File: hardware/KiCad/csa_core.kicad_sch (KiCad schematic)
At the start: 10 parts, among them Q1 2SK932, U5 AD8099ARD

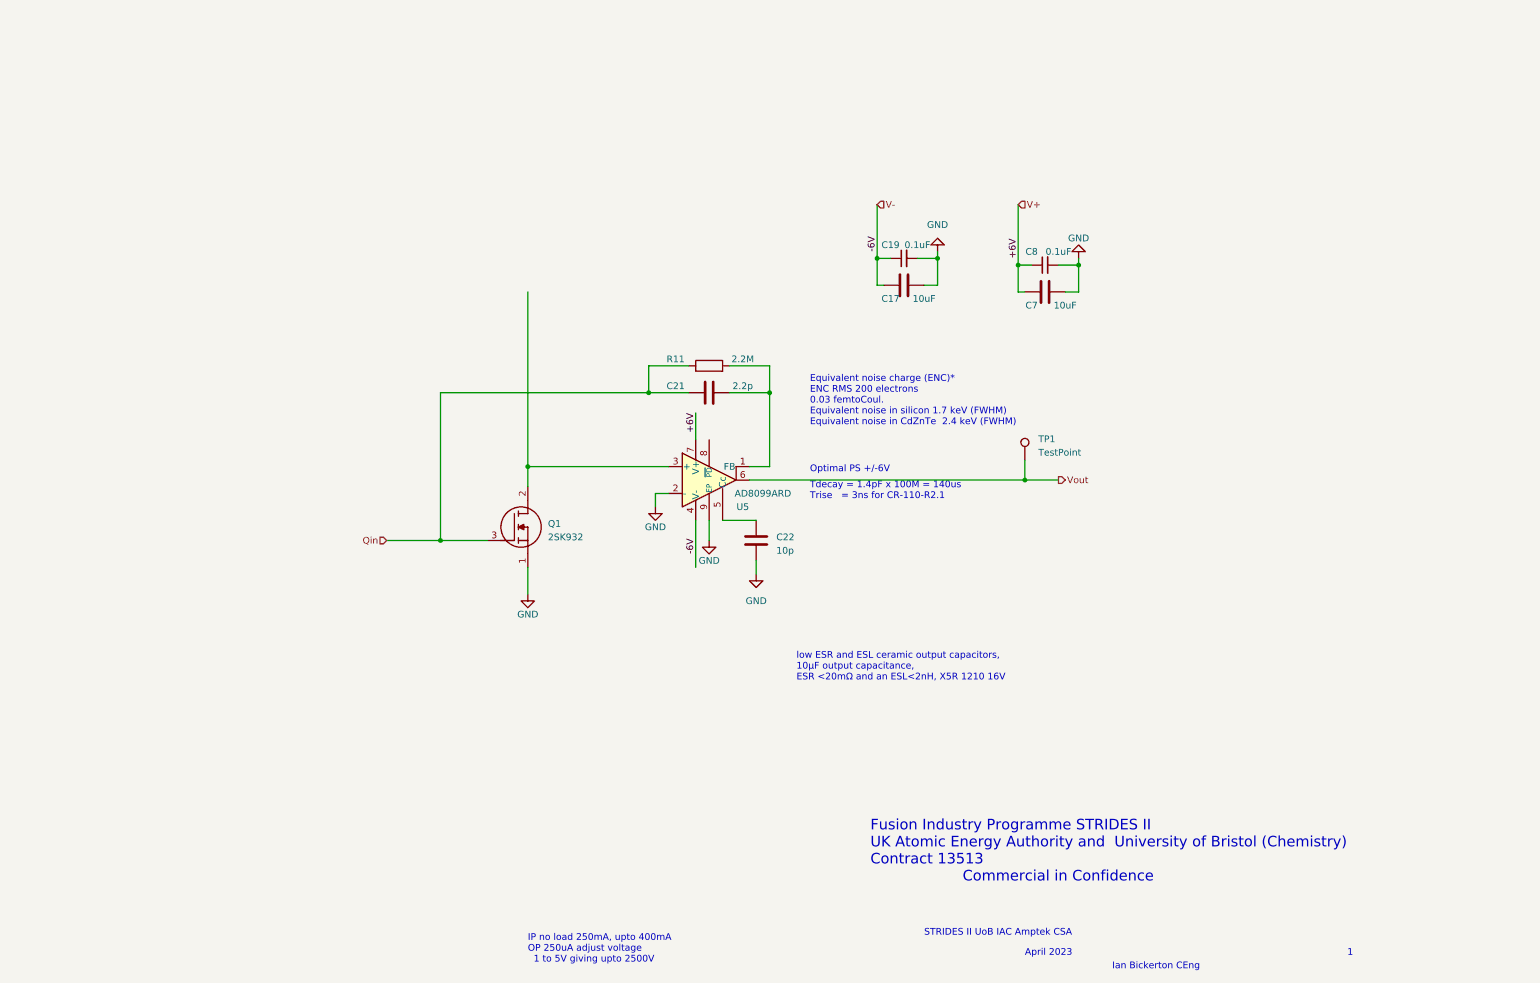
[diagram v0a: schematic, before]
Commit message: More schemataic tidying. Added a csa_core_simulation.kicad_pro to simulate CSA core. Tidied csa_core to make it simulatable, but needs work - OP analysis doesn't converge at the moment. (Need to fiddle with op-amp compensation??)
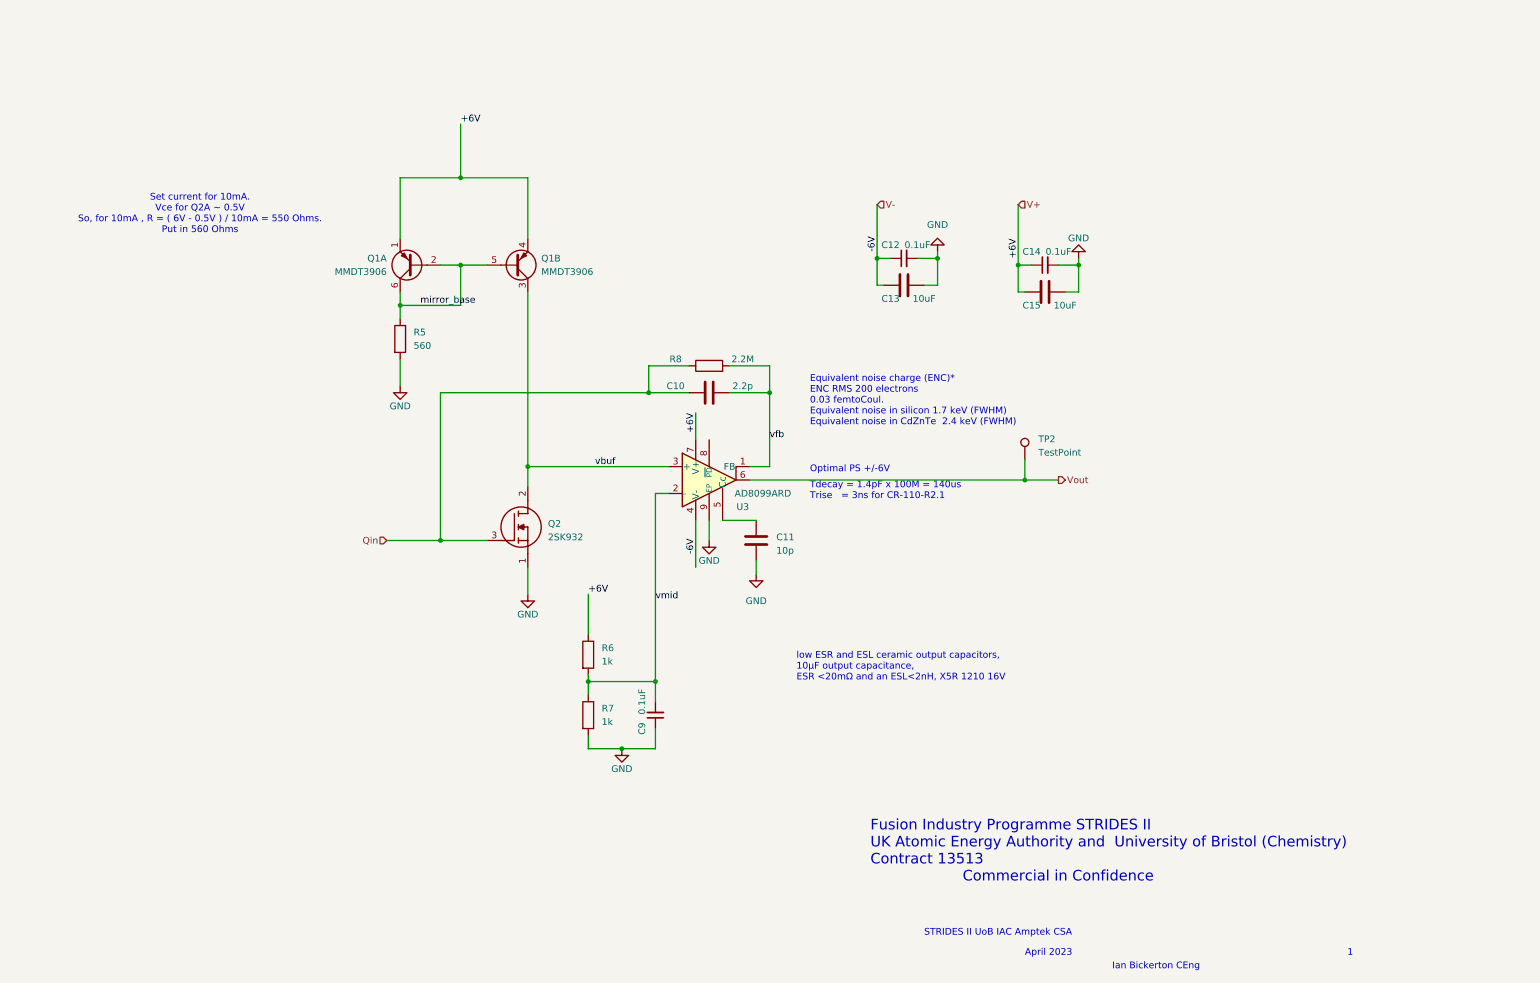
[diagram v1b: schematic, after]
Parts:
- added C9: 0.1uF, Capacitor_SMD:C_0805_2012Metric, symbol Device:C_Small
- added Q1: MMDT3906, Package_TO_SOT_SMD:SOT-363_SC-70-6, symbol Transistor_BJT:MMDT3906
- added R5: 560, Resistor_SMD:R_0603_1608Metric, symbol Device:R
- added R6, R7: 1k, Resistor_SMD:R_0603_1608Metric, symbol Device:R
- C11: renamed from C22; footprint (none) -> Capacitor_SMD:C_0603_1608Metric
- renumbered C21 to C10, C19 to C12, C17 to C13, C8 to C14, C7 to C15, Q1 to Q2, R11 to R8, TP1 to TP2, U5 to U3
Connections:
- net GND: now also C9.1, R5.2, R7.2; no longer U3.2 (-)
- net V+: now also Q1.1 (E1), Q1.4 (E2), R6.1
- net vfb: now reaches C10.2, R8.2, U3.1 (FB)
- net vbuf: now reaches Q2.2 (D), U3.3 (+)
- net vbuf: now also Q1.3 (C2)
- new net mirror_base: Q1.2 (B1), Q1.5 (B2), Q1.6 (C1), R5.1
- new net vmid: C9.2, R6.2, R7.1, U3.2 (-)
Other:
- note added: "Set current for 10mA. Vce for Q2A ~ 0.5V So, for 10mA , R = ( 6V - 0.5V ) / 10mA = 550 Ohms. Put in 560 Ohms"
- note removed: "IP no load 250mA, upto 400mA OP 250uA adjust voltage 1 to 5V giving upto 2500V"

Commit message: Added lead-lag compenstation after JFET which seems to stabilize loop in simulation. Added CR-RC shaping/amplification. Committing changes before starting simulation of shapers
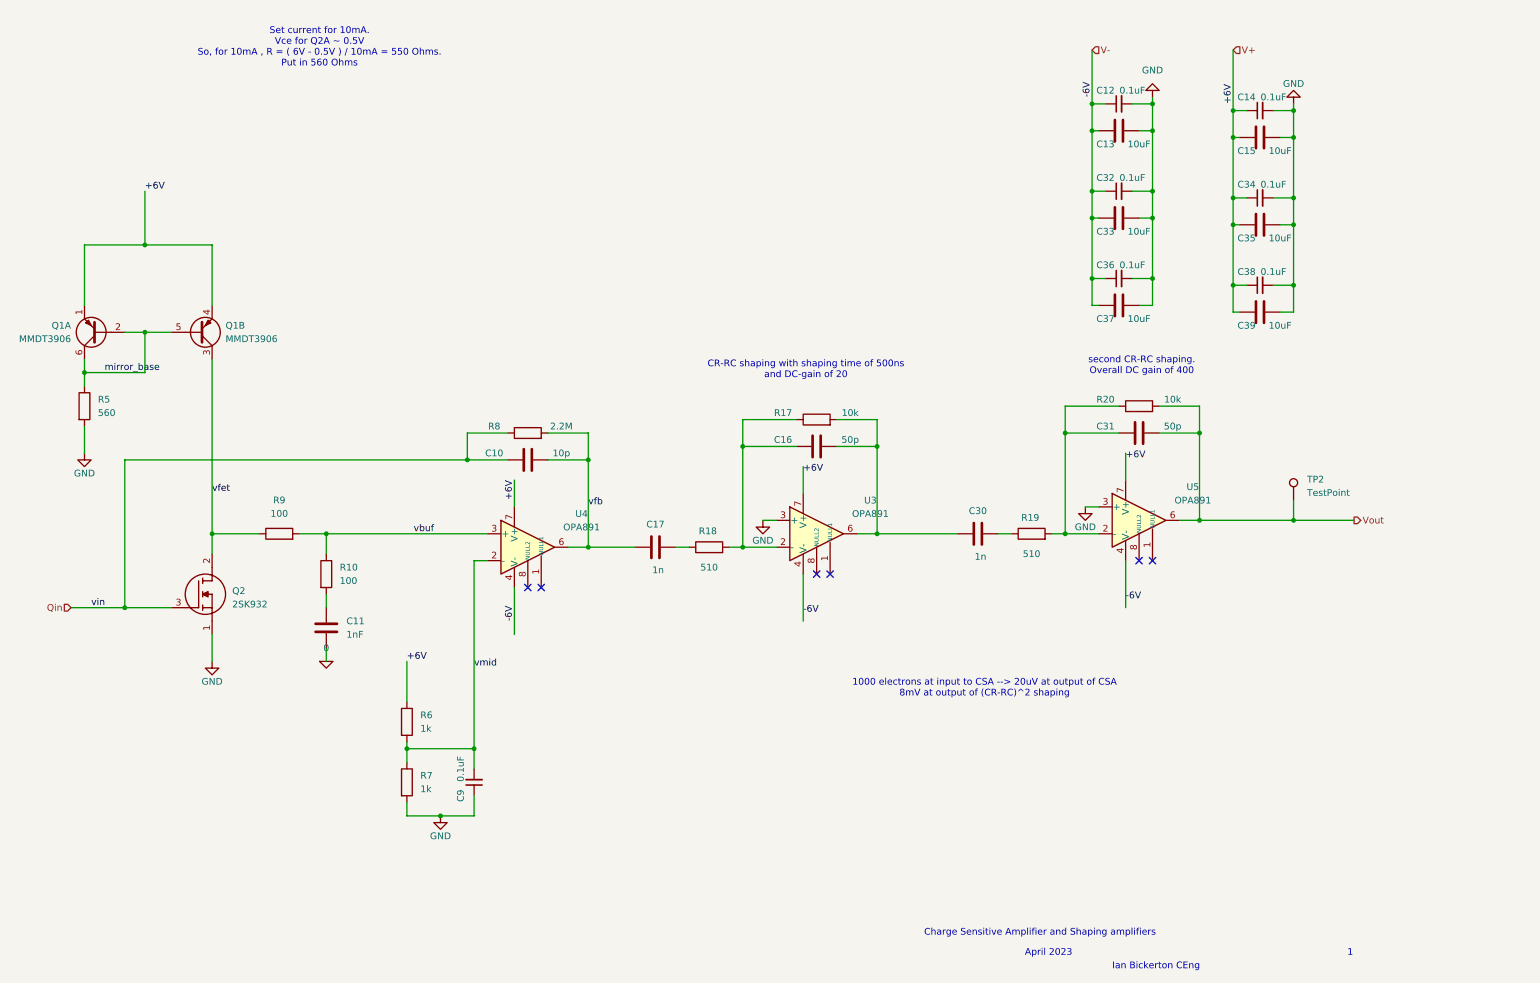
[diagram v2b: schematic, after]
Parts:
- removed U3: AD8099ARD, AD8099:RD_8_1_ADI, symbol AD8099:AD8099ARD
- added C16, C31: 50p, Resistor_SMD:R_0603_1608Metric_Pad0.98x0.95mm_HandSolder, symbol Device:C
- added C17, C30: 1n, Resistor_SMD:R_0603_1608Metric_Pad0.98x0.95mm_HandSolder, symbol Device:C
- added C32, C34, C36, C38: 0.1uF, Capacitor_SMD:C_0805_2012Metric, symbol Device:C_Small
- added C33, C35, C37, C39: 10uF, Capacitor_SMD:C_0805_2012Metric, symbol Device:C
- added R10, R9: 100, symbol Device:R
- added R17, R20: 10k, Resistor_SMD:R_0603_1608Metric_Pad0.98x0.95mm_HandSolder, symbol Device:R
- added R18, R19: 510, Resistor_SMD:R_0603_1608Metric_Pad0.98x0.95mm_HandSolder, symbol Device:R
- added U3, U4, U5: OPA891, Package_SO:SOIC-8_7.5x5.85mm_P1.27mm, symbol OPA891:OPA891
- C10: value 2.2p -> 10p
- C11: value 10p -> 1nF; footprint Capacitor_SMD:C_0603_1608Metric -> (none)
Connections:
- net GND: now also C32.2, C33.2, C34.2, C35.2, C36.2, C37.2, C38.2, C39.2, U3.3 (+), U5.3 (+); no longer C11.2
- net V+: now also C34.1, C35.1, C38.1, C39.1, U3.7 (V+), U4.7 (V+), U5.7 (V+)
- net V-: now also C32.1, C33.1, C36.1, C37.1, U3.4 (V-), U4.4 (V-), U5.4 (V-)
- net Vout: now also C31.2, R20.2, U5.6
- net vbuf: now also R10.1, R9.2, U4.3 (+); no longer Q1.3 (C2), Q2.2 (D)
- net vfb: now also C17.1, U4.6
- net vmid: now also U4.2 (-)
- net at C11.1: now also R10.2
- new net: C31.1, R19.2, R20.1, U5.2 (-)
- new net: C16.1, R17.1, R18.2, U3.2 (-)
- new net: C16.2, C30.1, R17.2, U3.6
- new net: C17.2, R18.1
- new net: C30.2, R19.1
- new net 0: C11.2
- new net vfet: Q1.3 (C2), Q2.2 (D), R9.1
- no-connect marks 0 -> 6
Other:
- note added: "1000 electrons at input to CSA --> 20uV at output of CSA 8mV at output of (CR-RC)^2 shaping"
- note added: "CR-RC shaping with shaping time of 500ns and DC-gain of 20"
- note added: "Charge Sensitive Amplifier and Shaping amplifiers"
- note added: "second CR-RC shaping. Overall DC gain of 400"
- note removed: "Equivalent noise charge (ENC)* ENC RMS 200 electrons 0.03 femtoCoul. Equivalent noise in silicon 1.7 keV (FWHM) Equivalent noise in CdZnTe 2.4 keV (FWHM)"
- note removed: "Fusion Industry Programme STRIDES II UK Atomic Energy Authority and University of Bristol (Chemistry) Contract 13513 Commercial in Confidence"
- note removed: "Optimal PS +/-6V"
- note removed: "STRIDES II UoB IAC Amptek CSA"
- note removed: "Tdecay = 1.4pF x 100M = 140us Trise = 3ns for CR-110-R2.1"
- note removed: "low ESR and ESL ceramic output capacitors, 10µF output capacitance, ESR <20mΩ and an ESL<2nH, X5R 1210 16V"
- moved on the sheet: C10, C12, C13, C14, C15, C9, Q1A, Q1B, Q2, R5, R6, R7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

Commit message: End of day save. Just needs voids added to planes to reduce capacitance
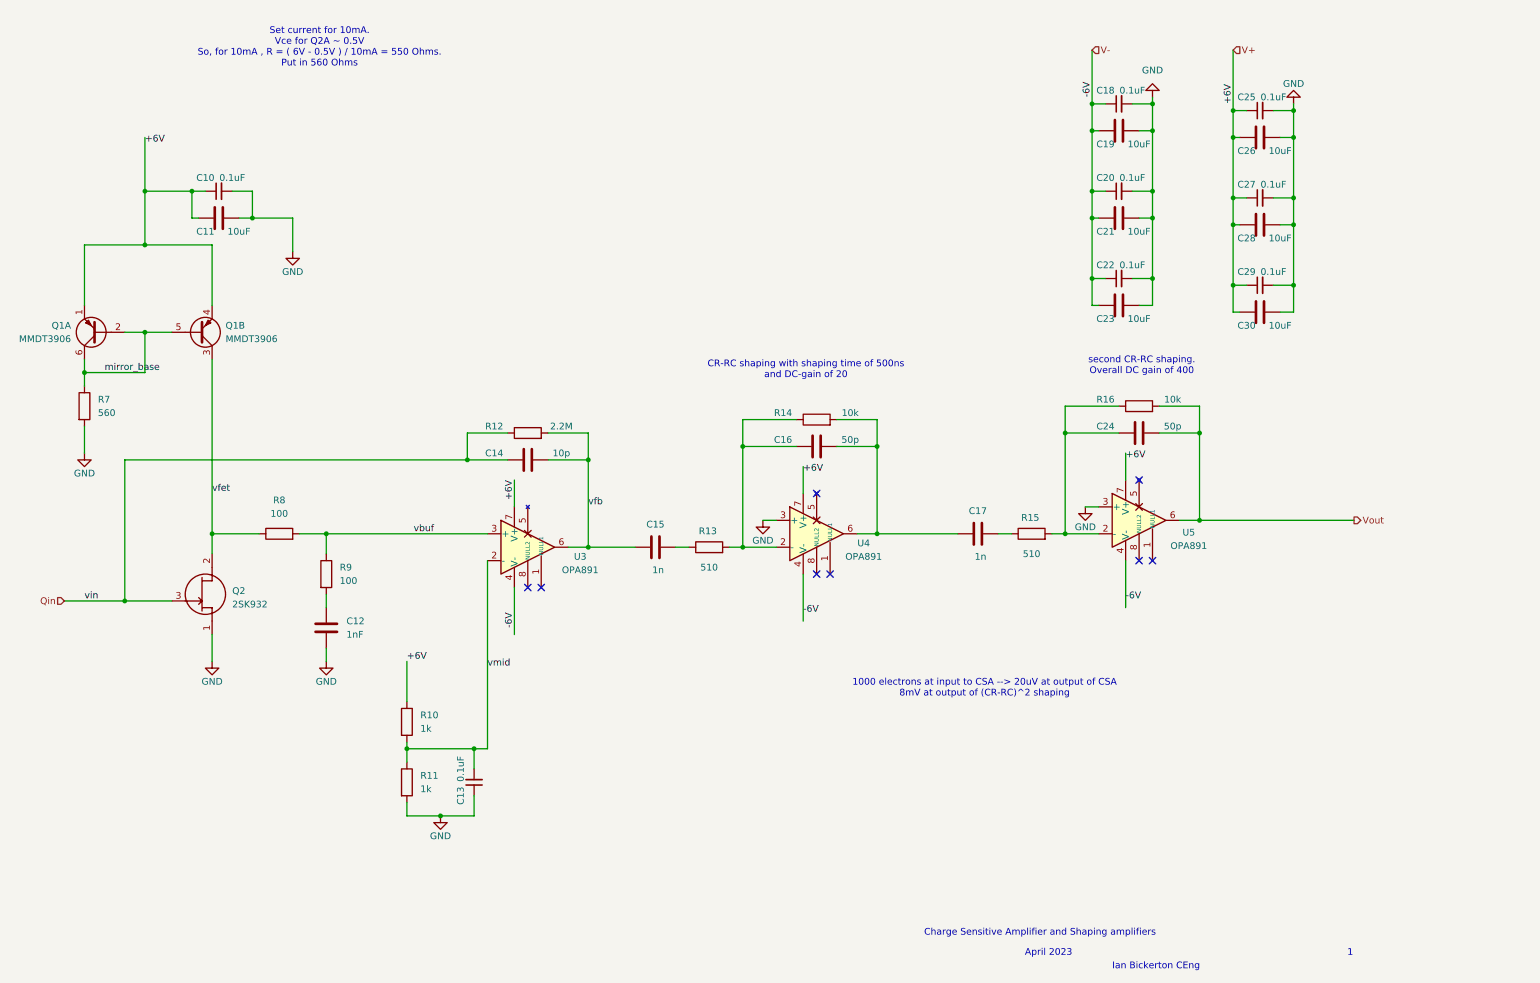
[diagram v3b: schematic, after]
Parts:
- removed TP2: TestPoint, TestPoint:TestPoint_Pad_2.0x2.0mm, symbol Connector:TestPoint
- added C10: 0.1uF, Capacitor_SMD:C_0805_2012Metric, symbol Device:C_Small
- added C11: 10uF, Capacitor_SMD:C_0805_2012Metric, symbol Device:C
- C12: renamed from C11; footprint (none) -> Capacitor_SMD:C_0603_1608Metric_Pad1.08x0.95mm_HandSolder
- R8: renamed from R9; footprint (none) -> Resistor_SMD:R_0603_1608Metric_Pad0.98x0.95mm_HandSolder
- R9: renamed from R10; footprint (none) -> Resistor_SMD:R_0603_1608Metric_Pad0.98x0.95mm_HandSolder
- U3: renamed from U4; footprint Package_SO:SOIC-8_7.5x5.85mm_P1.27mm -> Package_SO:SOIC-8_5.275x5.275mm_P1.27mm
- U4: renamed from U3; footprint Package_SO:SOIC-8_7.5x5.85mm_P1.27mm -> Package_SO:SOIC-8_5.275x5.275mm_P1.27mm
- U5: footprint Package_SO:SOIC-8_7.5x5.85mm_P1.27mm -> Package_SO:SOIC-8_5.275x5.275mm_P1.27mm
- renumbered C9 to C13, C10 to C14, C17 to C15, C30 to C17, C12 to C18, C13 to C19, C32 to C20, C33 to C21, C36 to C22, C37 to C23, C31 to C24, C14 to C25, C15 to C26, C34 to C27, C35 to C28, C38 to C29, C39 to C30, R6 to R10, R7 to R11, R8 to R12, R18 to R13, R17 to R14, R19 to R15, R20 to R16, R5 to R7
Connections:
- net 0 is gone; now on net GND: C12.2
- net GND: now also C10.2, C11.2
- net V+: now also C10.1, C11.1
- no-connect marks 6 -> 8

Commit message: Generated artwork
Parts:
- removed Q1: MMDT3906, Package_TO_SOT_SMD:SOT-363_SC-70-6, symbol Transistor_BJT:MMDT3906
- added C31: 0.1uF, Capacitor_SMD:C_0805_2012Metric, symbol Device:C_Small
- added L1: Wurth 742792651, Inductor_SMD:L_0603_1608Metric_Pad1.05x0.95mm_HandSolder, symbol Device:L_Ferrite_Small
- added Q1: BFS20, Package_TO_SOT_SMD:SOT-23, symbol BFS20:BFS20
- added R19, R20: 1k, Resistor_SMD:R_0603_1608Metric_Pad0.98x0.95mm_HandSolder, symbol Device:R
- added R21: 10, Resistor_SMD:R_0603_1608Metric_Pad0.98x0.95mm_HandSolder, symbol Device:R
- C12: value 1nF -> 1n
- R10: footprint Resistor_SMD:R_0603_1608Metric -> Resistor_SMD:R_0603_1608Metric_Pad0.98x0.95mm_HandSolder
- R11: value 1k -> 1.5k; footprint Resistor_SMD:R_0603_1608Metric -> Resistor_SMD:R_0603_1608Metric_Pad0.98x0.95mm_HandSolder
- R7: value 560 -> 1.2k; footprint Resistor_SMD:R_0603_1608Metric -> Resistor_SMD:R_0603_1608Metric_Pad0.98x0.95mm_HandSolder
- R8: value 100 -> 1k
- R9: value 100 -> 10
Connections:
- net GND: now also C31.1, R19.2; no longer R7.2
- net V+: now also R21.1; no longer C10.1, C11.1
- net mirror_base: no longer names the net of R7.1
- net mirror_base: now also C10.1, C11.1, L1.2, R20.1
- net vfet renamed vc
- net vc: now also Q1.3 (C), R20.2; no longer Q2.2 (D)
- new net: L1.1, R21.2
- new net vbase: C31.2, Q1.1 (B), R19.1, R7.2
- new net ve: Q1.2 (E), Q2.2 (D)
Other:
- note added: "Put in LC filter for cascode supply. Add resistor in case damping is needed"
- note added: "Set current for 4mA. Feedback sets Vc = 6V, so voltage across R20=4V."
- note removed: "Set current for 10mA. Vce for Q2A ~ 0.5V So, for 10mA , R = ( 6V - 0.5V ) / 10mA = 550 Ohms. Put in 560 Ohms"
- moved on the sheet: C10, C11, C12, R8, R9

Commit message: Produced gerbers
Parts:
- C16, C24: value 50p -> 47p
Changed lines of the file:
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@@
 			)
 		)
-		(property "Value" "50p"
+		(property "Value" "47p"
 			(at 237.49 93.98 90)
 			(effects
@@
 			)
 		)
-		(property "Value" "50p"
+		(property "Value" "47p"
 			(at 176.53 96.52 90)
 			(effects
